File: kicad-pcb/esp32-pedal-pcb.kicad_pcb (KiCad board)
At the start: 4 copper layers, 216 x 25 mm, 49 parts, among them J1 USB_C_Receptacle_USB2.0_14P, J2 Conn_01x03, J3 Conn_01x03, Q1 Q_PMOS_GSD, SW1 SW_SPST, SW2 SW_SPDT, U1 MCP73871, U2 TLV75733PDBV, U3 ESP32-S3-WROOM-1, U4 TPD2EUSB30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

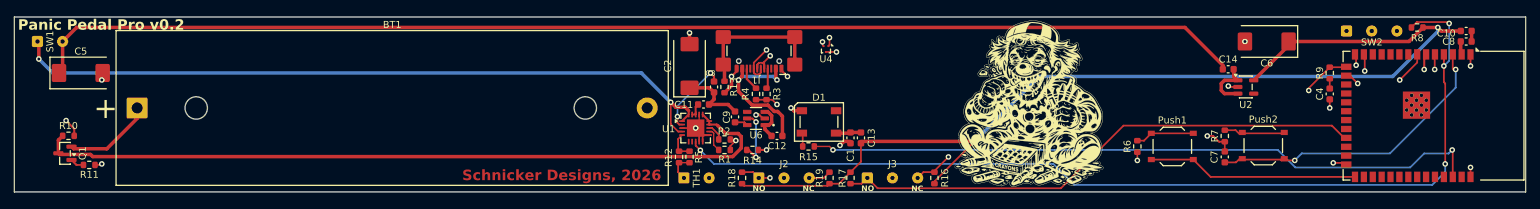
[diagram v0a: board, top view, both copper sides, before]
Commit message: Update KiCad PCB project files and backups
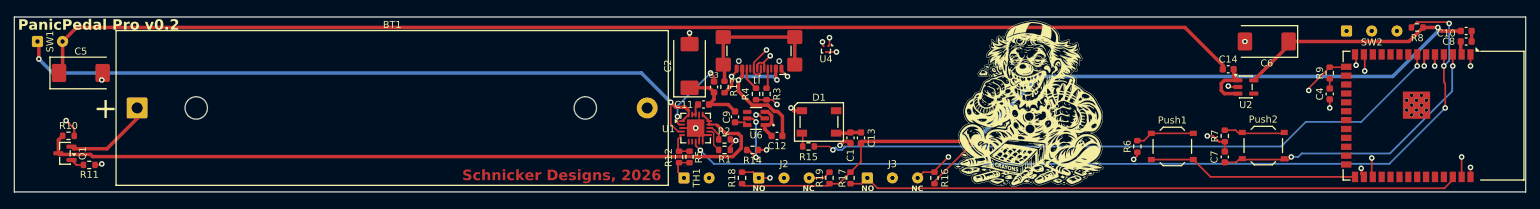
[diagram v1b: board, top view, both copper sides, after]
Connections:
- U3 pad 16: Net-(J3-Pin_3) -> unconnected-(U3-GPIO46-Pad16)
- U3 pad 23: Net-(J3-Pin_1) -> unconnected-(U3-GPIO21-Pad23)
- U3 pad 26: Net-(J2-Pin_3) -> unconnected-(U3-GPIO45-Pad26)
- U3 pad 28: unconnected-(U3-SPIIO6/GPIO35/FSPID/SUBSPID-Pad28) -> Net-(J2-Pin_3)
- U3 pad 29: unconnected-(U3-SPIIO7/GPIO36/FSPICLK/SUBSPICLK-Pad29) -> Net-(J3-Pin_3)
- U3 pad 38: /Led DIN -> Net-(J3-Pin_1)
- U3 pad 39: unconnected-(U3-GPIO1/TOUCH1/ADC1_CH0-Pad39) -> Net-(J2-Pin_1)
- U3 pad 7: Net-(J2-Pin_1) -> /Led DIN
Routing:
- net Net-(J3-Pin_1): track 76.2 -> 88.0 mm
- net Net-(J3-Pin_3): track 70.7 -> 79.6 mm
- net Net-(U1-STAT1/~{LBO}): track 139.9 -> 132.0 mm
- net Net-(J2-Pin_3): track 81.9 -> 86.0 mm
- net /Led DIN: track 97.3 -> 93.4 mm
- net Net-(J2-Pin_1): track 104.0 -> 107.3 mm
- net Net-(SW2-C): track 9.96 -> 9.14 mm
- net /RESET: track 42.0 -> 41.3 mm
- net Net-(SW2-A): track 15.6 -> 16.2 mm
- net unconnected-(U3-GPIO46-Pad16): track 0.00 -> 0.52 mm
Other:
- board text added: "PanicPedal Pro v0.2"
- board text removed: "Panic Pedal Pro v0.2"
